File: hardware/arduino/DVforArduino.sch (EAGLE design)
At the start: 55 parts, among them Q1 2N7000, Q2 2N7000, U1 CML-MICRO_CMX589AE2, U2 CML-MICRO_CMX589AP4, U3 OPAMP-DUALDIP, Y1 4.9152MHz

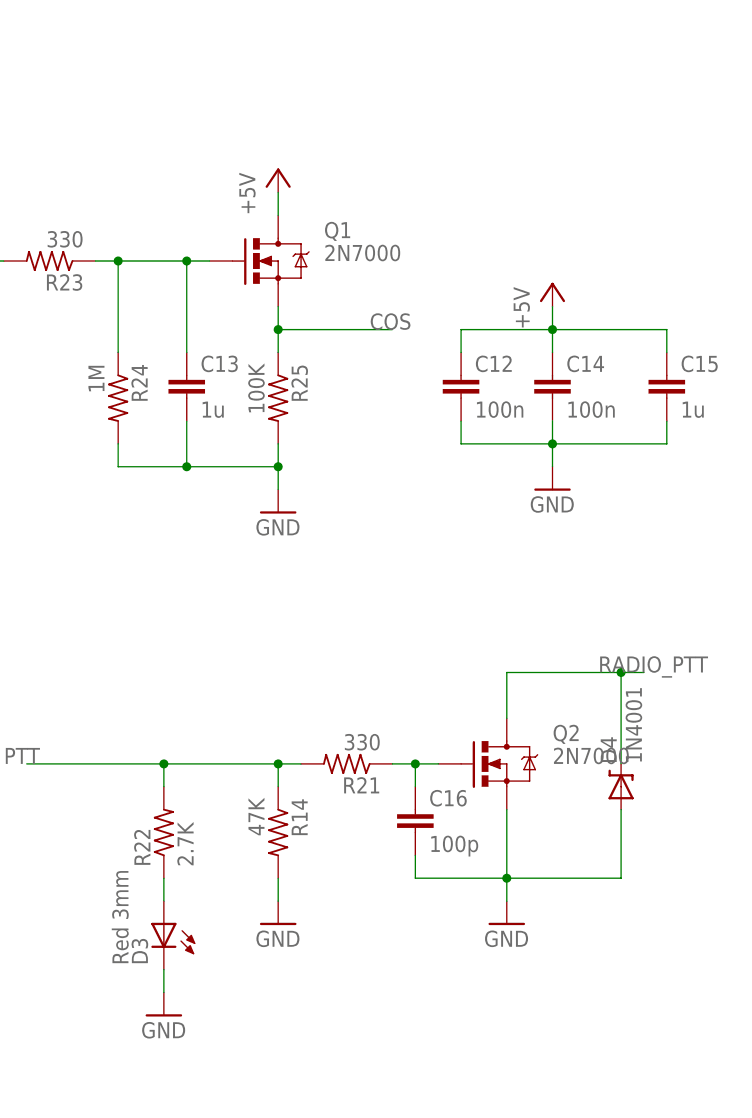
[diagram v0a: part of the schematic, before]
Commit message: 
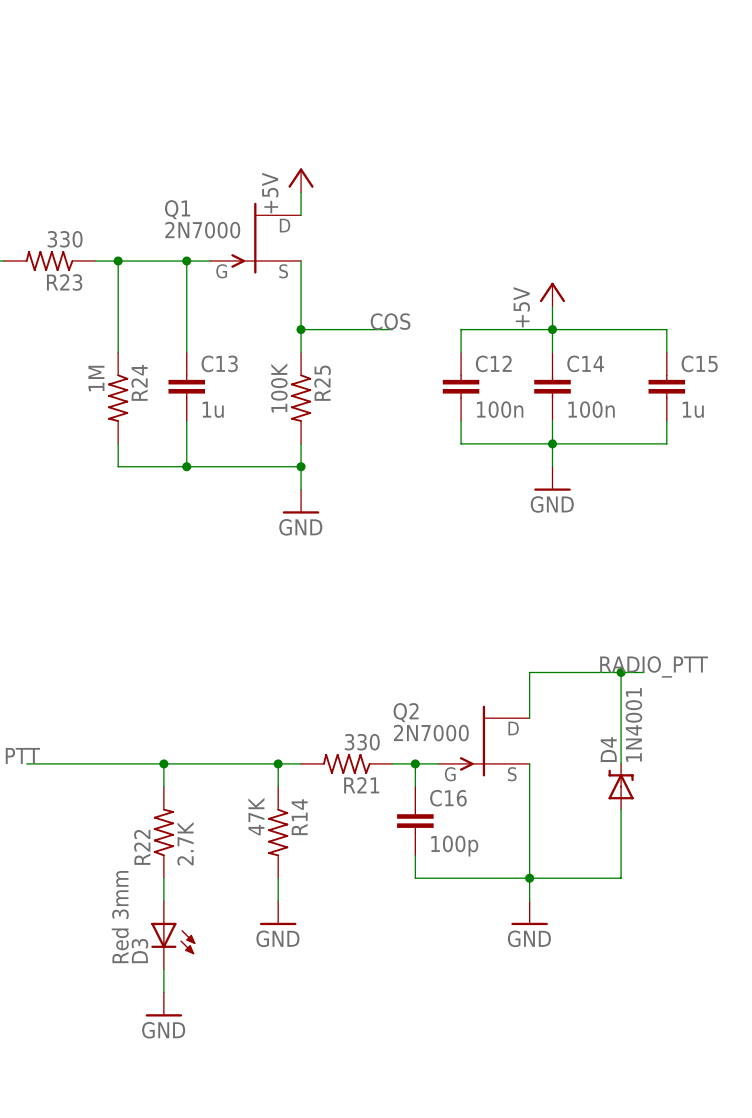
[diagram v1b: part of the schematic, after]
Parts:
- Q1, Q2: device SparkFun-DiscreteSemi:MOSFET-NCHANNELBS170 -> transistor-fet:2N3819
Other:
- moved on the sheet: R25
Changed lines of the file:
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@@
 <?xml version="1.0" encoding="utf-8"?>
 <!DOCTYPE eagle SYSTEM "eagle.dtd">
-<eagle version="6.3">
+<eagle version="6.4">
 <drawing>
 <settings>
@@
 <part name="D3" library="adafruit" deviceset="LED" device="3MM" value="Red 3mm"/>
 <part name="R22" library="resistor" deviceset="R-US_" device="0204/2V" value="2.7K"/>
-<part name="Q1" library="SparkFun-DiscreteSemi" deviceset="MOSFET-NCHANNEL" device="BS170" value="2N7000"/>
+<part name="Q1" library="transistor-fet" deviceset="2N3819" device="" value="2N7000"/>
 <part name="R23" library="resistor" deviceset="R-US_" device="0204/2V" value="330"/>
 <part name="R24" library="resistor" deviceset="R-US_" device="0204/2V" value="1M"/>
@@
 <part name="GND13" library="supply1" deviceset="GND" device=""/>
 <part name="+3V5" library="supply1" deviceset="+3V3" device="" value="+5V"/>
-<part name="Q2" library="SparkFun-DiscreteSemi" deviceset="MOSFET-NCHANNEL" device="BS170" value="2N7000"/>
+<part name="Q2" library="transistor-fet" deviceset="2N3819" device="" value="2N7000"/>
 <part name="C12" library="capacitor-wima" deviceset="C" device="2,5-3" value="100n"/>
 <part name="U$1" library="creativecommons" deviceset="CC-BY-NC-SA" device=""/>
@@
 <instance part="RX" gate="G$1" x="63.5" y="177.8" rot="MR270"/>
 <instance part="R21" gate="G$1" x="325.12" y="78.74" rot="R180"/>
-<instance part="GND7" gate="1" x="342.9" y="60.96"/>
+<instance part="GND7" gate="1" x="345.44" y="60.96"/>
 <instance part="D3" gate="G$1" x="304.8" y="60.96" rot="MR0"/>
 <instance part="R22" gate="G$1" x="304.8" y="71.12" rot="R90"/>
-<instance part="Q1" gate="G$1" x="317.5" y="134.62"/>
+<instance part="Q1" gate="G$1" x="314.96" y="137.16"/>
 <instance part="R23" gate="G$1" x="292.1" y="134.62" rot="R180"/>
 <instance part="R24" gate="G$1" x="299.72" y="119.38" rot="R270"/>
-<instance part="GND10" gate="1" x="317.5" y="106.68"/>
+<instance part="GND10" gate="1" x="320.04" y="106.68"/>
 <instance part="GND11" gate="1" x="317.5" y="175.26"/>
-<instance part="R25" gate="G$1" x="317.5" y="119.38" rot="R270"/>
+<instance part="R25" gate="G$1" x="320.04" y="119.38" rot="R270"/>
 <instance part="C13" gate="G$1" x="307.34" y="121.92"/>
 <instance part="D1" gate="G$1" x="104.14" y="114.3" rot="MR0"/>
@@
 <instance part="GND12" gate="1" x="124.46" y="106.68"/>
 <instance part="FRAME1" gate="G$1" x="0" y="0"/>
-<instance part="+5V1" gate="G$1" x="317.5" y="144.78"/>
+<instance part="+5V1" gate="G$1" x="320.04" y="144.78"/>
 <instance part="+3V2" gate="G$1" x="317.5" y="200.66"/>
 <instance part="+3V4" gate="G$1" x="231.14" y="248.92"/>
@@
 <instance part="GND13" gate="1" x="170.18" y="38.1"/>
 <instance part="+3V5" gate="G$1" x="231.14" y="134.62"/>
-<instance part="Q2" gate="G$1" x="342.9" y="78.74"/>
+<instance part="Q2" gate="G$1" x="340.36" y="81.28"/>
 <instance part="C12" gate="G$1" x="337.82" y="121.92"/>
 <instance part="U$1" gate="G$1" x="320.04" y="5.08"/>
@@
 <segment>
 <pinref part="GND7" gate="1" pin="GND"/>
-<wire x1="342.9" y1="66.04" x2="342.9" y2="63.5" width="0.1524" layer="91"/>
-<junction x="342.9" y="66.04"/>
-<wire x1="332.74" y1="66.04" x2="342.9" y2="66.04" width="0.1524" layer="91"/>
-<wire x1="355.6" y1="66.04" x2="342.9" y2="66.04" width="0.1524" layer="91"/>
+<wire x1="345.44" y1="66.04" x2="345.44" y2="63.5" width="0.1524" layer="91"/>
+<junction x="345.44" y="66.04"/>
+<wire x1="332.74" y1="66.04" x2="345.44" y2="66.04" width="0.1524" layer="91"/>
+<wire x1="355.6" y1="66.04" x2="345.44" y2="66.04" width="0.1524" layer="91"/>
 <pinref part="C16" gate="G$1" pin="2"/>
 <wire x1="332.74" y1="68.58" x2="332.74" y2="66.04" width="0.1524" layer="91"/>
@@
 <wire x1="355.6" y1="66.04" x2="355.6" y2="73.66" width="0.1524" layer="91"/>
 <pinref part="Q2" gate="G$1" pin="S"/>
-<wire x1="342.9" y1="73.66" x2="342.9" y2="66.04" width="0.1524" layer="91"/>
+<wire x1="345.44" y1="78.74" x2="345.44" y2="66.04" width="0.1524" layer="91"/>
 </segment>
 <segment>
 <pinref part="R25" gate="G$1" pin="2"/>
 <pinref part="GND10" gate="1" pin="GND"/>
-<wire x1="317.5" y1="114.3" x2="317.5" y2="111.76" width="0.1524" layer="91"/>
+<wire x1="320.04" y1="114.3" x2="320.04" y2="111.76" width="0.1524" layer="91"/>
 <pinref part="R24" gate="G$1" pin="2"/>
-<wire x1="317.5" y1="111.76" x2="317.5" y2="109.22" width="0.1524" layer="91"/>
+<wire x1="320.04" y1="111.76" x2="320.04" y2="109.22" width="0.1524" layer="91"/>
 <wire x1="299.72" y1="114.3" x2="299.72" y2="111.76" width="0.1524" layer="91"/>
 <wire x1="299.72" y1="111.76" x2="307.34" y2="111.76" width="0.1524" layer="91"/>
 <pinref part="C13" gate="G$1" pin="2"/>
-<wire x1="307.34" y1="111.76" x2="317.5" y2="111.76" width="0.1524" layer="91"/>
+<wire x1="307.34" y1="111.76" x2="320.04" y2="111.76" width="0.1524" layer="91"/>
 <wire x1="307.34" y1="116.84" x2="307.34" y2="111.76" width="0.1524" layer="91"/>
 <junction x="307.34" y="111.76"/>
-<junction x="317.5" y="111.76"/>
+<junction x="320.04" y="111.76"/>
 </segment>
 <segment>
@@
 <pinref part="Q1" gate="G$1" pin="D"/>
 <pinref part="+5V1" gate="G$1" pin="+3V3"/>
-<wire x1="317.5" y1="139.7" x2="317.5" y2="142.24" width="0.1524" layer="91"/>
+<wire x1="320.04" y1="139.7" x2="320.04" y2="142.24" width="0.1524" layer="91"/>
 </segment>
 <segment>
@@
 <net name="RADIO_PTT" class="0">
 <segment>
-<wire x1="342.9" y1="88.9" x2="355.6" y2="88.9" width="0.1524" layer="91"/>
+<wire x1="345.44" y1="88.9" x2="355.6" y2="88.9" width="0.1524" layer="91"/>
 <label x="353.06" y="88.9" size="1.778" layer="95"/>
 <pinref part="D4" gate="G$1" pin="C"/>
@@
 <junction x="355.6" y="88.9"/>
 <pinref part="Q2" gate="G$1" pin="D"/>
-<wire x1="342.9" y1="88.9" x2="342.9" y2="83.82" width="0.1524" layer="91"/>
+<wire x1="345.44" y1="88.9" x2="345.44" y2="83.82" width="0.1524" layer="91"/>
 </segment>
 <segment>
@@
 <segment>
 <pinref part="R25" gate="G$1" pin="1"/>
-<wire x1="317.5" y1="127" x2="317.5" y2="124.46" width="0.1524" layer="91"/>
-<wire x1="317.5" y1="127" x2="330.2" y2="127" width="0.1524" layer="91"/>
+<wire x1="320.04" y1="127" x2="320.04" y2="124.46" width="0.1524" layer="91"/>
+<wire x1="320.04" y1="127" x2="330.2" y2="127" width="0.1524" layer="91"/>
 <label x="327.66" y="127" size="1.778" layer="95"/>
 <pinref part="Q1" gate="G$1" pin="S"/>
-<wire x1="317.5" y1="129.54" x2="317.5" y2="127" width="0.1524" layer="91"/>
-<junction x="317.5" y="127"/>
-</segment>
-<segment>
+<wire x1="320.04" y1="134.62" x2="320.04" y2="127" width="0.1524" layer="91"/>
+<junction x="320.04" y="127"/>
+</segment>
+<segment>

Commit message: 
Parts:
- added C18: 10u, capacitor-wima:C2,5-3
- added PRG: DNI, resistor:R-US_0204/2V
- D4: value 1N4001 -> DNI
- U1: device 12_dollar:AIS_MK2_CML-MICRO_CMX589AE2 -> mylibrary:AIS_MK2_CML-MICRO_CMX589AE2
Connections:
- new net N$6: C18.1, PRG.1
- new net RESET: JP10.1, PRG.2
- net +3V3: now also C18.2, U1.BT, U2.BT
- net GND: no longer U1.BT, U2.BT
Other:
- moved on the sheet: C1, C7, C8, D2, D4, JP10, JP2, JP7, JP8, JP9, R27
